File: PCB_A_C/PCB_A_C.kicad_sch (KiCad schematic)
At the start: 18 parts, among them J1 Conn_01x08_Socket, J2 Conn_01x04, J3 Screw_Terminal_01x02, SW1 SW_Push, SW2 SW_Push, SW3 SW_Push, SW4 SW_Push, SW5 SW_Push, U1 DHT11, U2 MSP430G2553IN20, Y0 32kHz

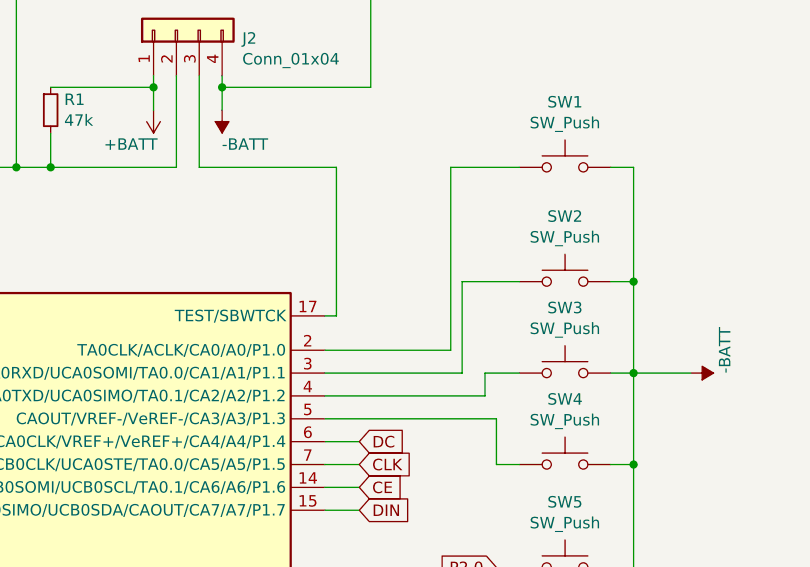
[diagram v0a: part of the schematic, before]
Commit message: Implemented battery level monitor. Updated readme
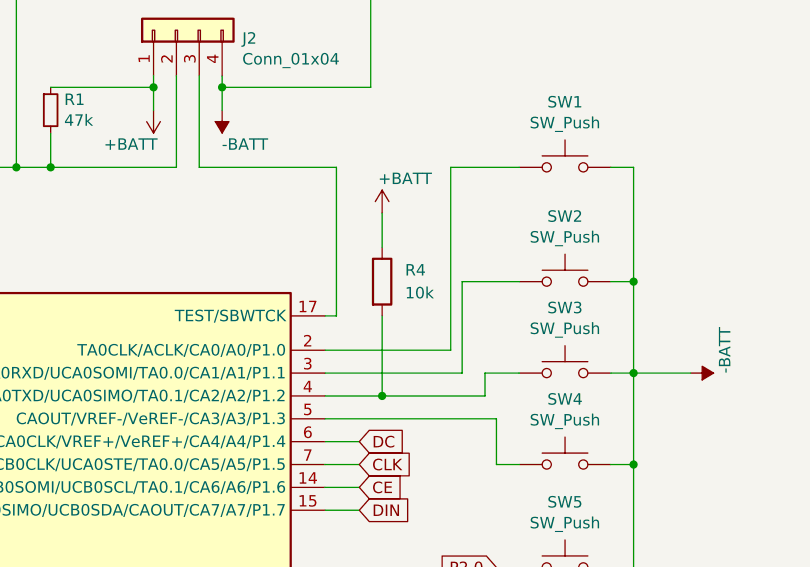
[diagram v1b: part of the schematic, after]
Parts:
- added R4: 10k, Resistor_SMD:R_1210_3225Metric_Pad1.30x2.65mm_HandSolder, symbol Device:R
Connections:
- net +BATT: now also R4.1
- net at SW3.1, U2.4 (UCA0TXD/UCA0SIMO/TA0.1/CA2/A2/P1.2): now also R4.2
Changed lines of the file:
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@@
   (junction (at 63.5 93.98) (diameter 0) (color 0 0 0 0)
   )
+  (junction (at 201.93 85.09) (diameter 0) (color 0 0 0 0)
+  )
   (wire (pts (xy 93.98 106.68) (xy 106.68 106.68))
     (stroke (width 0) (type default))
   )
-  (wire (pts (xy 195.58 85.09) (xy 213.36 85.09))
+  (wire (pts (xy 195.58 85.09) (xy 201.93 85.09))
     (stroke (width 0) (type default))
   )
@@
     (stroke (width 0) (type default))
   )
+  (wire (pts (xy 201.93 76.2) (xy 201.93 85.09))
+    (stroke (width 0) (type default))
+  )
   (wire (pts (xy 106.68 66.04) (xy 106.68 59.69))
     (stroke (width 0) (type default))
@@
     (stroke (width 0) (type default))
   )
+  (wire (pts (xy 201.93 64.77) (xy 201.93 68.58))
+    (stroke (width 0) (type default))
+  )
   (wire (pts (xy 152.4 69.85) (xy 152.4 68.58))
     (stroke (width 0) (type default))
@@
   )
   (wire (pts (xy 71.12 78.74) (xy 71.12 85.09))
+    (stroke (width 0) (type default))
+  )
+  (wire (pts (xy 201.93 85.09) (xy 213.36 85.09))
     (stroke (width 0) (type default))
   )
@@
     )
   )
+  (symbol (lib_id "Device:R") (at 201.93 72.39 0) (unit 1)
+    (in_bom yes) (on_board yes) (dnp no) (fields_autoplaced)
+    (property "Reference" "R4" (at 204.47 71.12 0)
+      (effects (font (size 1.27 1.27)) (justify left))
+    )
+    (property "Value" "10k" (at 204.47 73.66 0)
+      (effects (font (size 1.27 1.27)) (justify left))
+    )
+    (property "Footprint" "Resistor_SMD:R_1210_3225Metric_Pad1.30x2.65mm_HandSolder" (at 200.152 72.39 90)
+      (effects (font (size 1.27 1.27)) hide)
+    )
+    (property "Datasheet" "~" (at 201.93 72.39 0)
+      (effects (font (size 1.27 1.27)) hide)
+    )
+    (pin "1")
+    (pin "2")
+    (instances
+      (project "PCB_A_C"
+        (path "/53a6b296-7a3a-4e15-8fef-b2c22685c773"
+          (reference "R4") (unit 1)
+        )
+      )
+    )
+  )
   (symbol (lib_id "Device:LED") (at 72.39 91.44 0) (unit 1)
     (in_bom yes) (on_board yes) (dnp no)
@@
         )
       )
+    )
+  )
+  (symbol (lib_id "power:+BATT") (at 201.93 64.77 0) (unit 1)
+    (in_bom yes) (on_board yes) (dnp no)
+    (property "Reference" "#PWR03" (at 201.93 68.58 0)
+      (effects (font (size 1.27 1.27)) hide)
+    )
+    (property "Value" "+BATT" (at 204.47 60.96 0)
+      (effects (font (size 1.27 1.27)))
+    )
+    (property "Footprint" "" (at 201.93 64.77 0)
+      (effects (font (size 1.27 1.27)) hide)
+    )
+    (property "Datasheet" "" (at 201.93 64.77 0)
+      (effects (font (size 1.27 1.27)) hide)
+    )
+    (pin "1")
+    (instances
+      (project "PCB_A_C"
+        (path "/53a6b296-7a3a-4e15-8fef-b2c22685c773"
+          (reference "#PWR03") (unit 1)
+        )
+      )
